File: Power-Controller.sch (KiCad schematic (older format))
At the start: 41 parts, among them P1 USB_B, U1 FT232H, U2 93LC56BT-I/OT, U3 ACPL-247-500E, U4 ACPL-247-500E, Y1 12MHz

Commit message: Change the footprint of 4.7uF capacitors to 1206 to conform to the other circuits (This size of the footprint is used since 2015)
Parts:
- C11, C13, C15, C17: footprint Capacitors_SMD:C_0603 -> SMD_Packages:SMD-1206_Pol
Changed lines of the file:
@@
 F 0 "C17" H 5110 2470 50  0000 L CNN
 F 1 "4.7uF" H 5110 2320 50  0000 L CNN
-F 2 "Capacitors_SMD:C_0603" H 5100 2400 50  0001 C CNN
+F 2 "SMD_Packages:SMD-1206_Pol" H 5100 2400 50  0001 C CNN
 F 3 "" H 5100 2400 50  0000 C CNN
 	1    5100 2400
@@
 F 0 "C11" H 3410 2870 50  0000 L CNN
 F 1 "4.7uF" H 3410 2720 50  0000 L CNN
-F 2 "Capacitors_SMD:C_0603" H 3400 2800 50  0001 C CNN
+F 2 "SMD_Packages:SMD-1206_Pol" H 3400 2800 50  0001 C CNN
 F 3 "" H 3400 2800 50  0000 C CNN
 	1    3400 2800
@@
 F 0 "C15" H 5110 1970 50  0000 L CNN
 F 1 "4.7uF" H 5110 1820 50  0000 L CNN
-F 2 "Capacitors_SMD:C_0603" H 5100 1900 50  0001 C CNN
+F 2 "SMD_Packages:SMD-1206_Pol" H 5100 1900 50  0001 C CNN
 F 3 "" H 5100 1900 50  0000 C CNN
 	1    5100 1900
@@
 F 0 "C13" H 4160 1970 50  0000 L CNN
 F 1 "4.7uF" H 4160 1820 50  0000 L CNN
-F 2 "Capacitors_SMD:C_0603" H 4150 1900 50  0001 C CNN
+F 2 "SMD_Packages:SMD-1206_Pol" H 4150 1900 50  0001 C CNN
 F 3 "" H 4150 1900 50  0000 C CNN
 	1    4150 1900

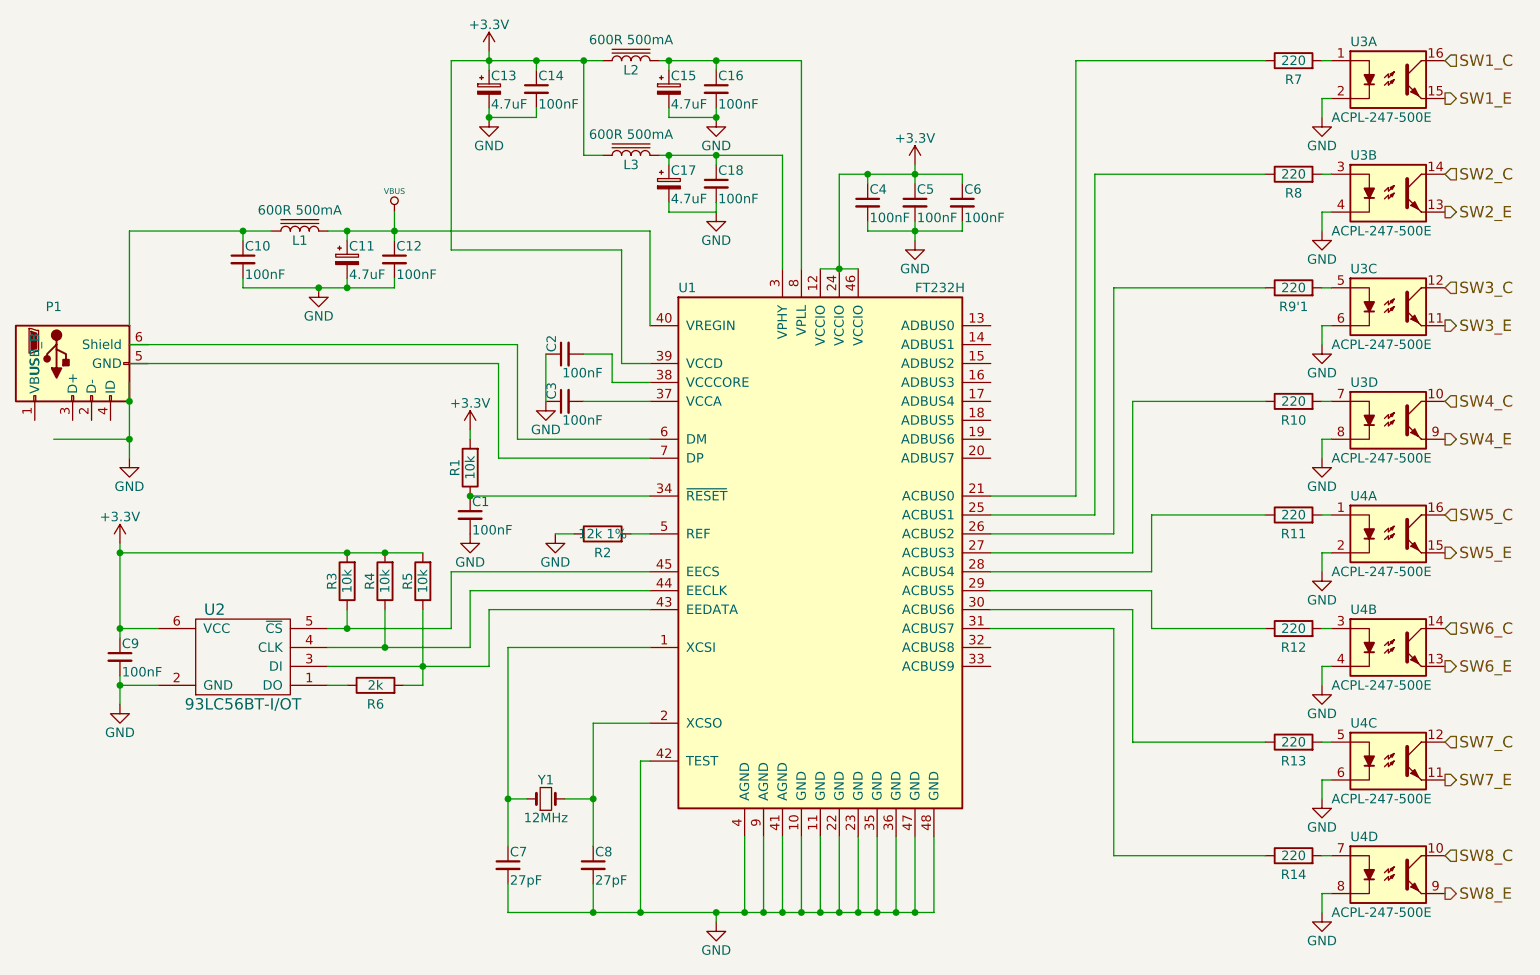
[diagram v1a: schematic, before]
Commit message: Change some R values and C footprints to conform with the Peripheral Bridge module.
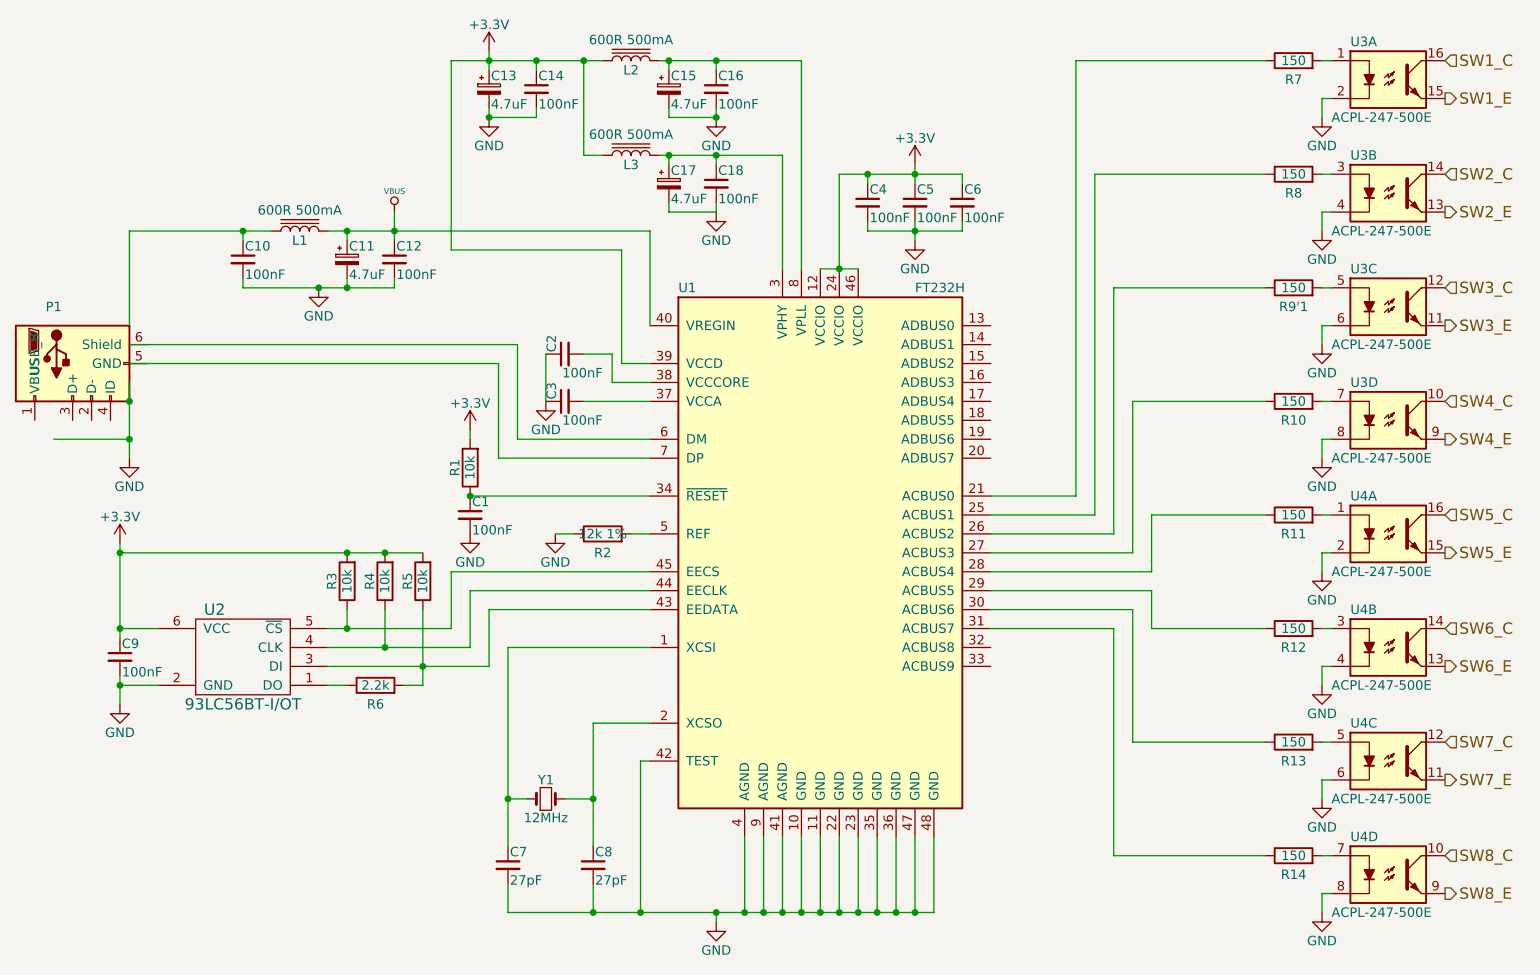
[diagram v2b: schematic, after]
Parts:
- C11: footprint SMD_Packages:SMD-1206_Pol -> MMZ1608S601A-CT
- C13, C15, C17: footprint SMD_Packages:SMD-1206_Pol -> Capacitors_SMD:C_0805
- R10, R11, R12, R13, R14, R7, R8, R9'1: value 220 -> 150
- R6: value 2k -> 2.2k
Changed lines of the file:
@@
 P 3550 5050
 F 0 "R6" V 3450 5050 50  0000 C CNN
-F 1 "2k" V 3550 5050 50  0000 C CNN
+F 1 "2.2k" V 3550 5050 50  0000 C CNN
 F 2 "Resistors_SMD:R_0603" V 3480 5050 30  0001 C CNN
 F 3 "" H 3550 5050 30  0000 C CNN
@@
 F 0 "C17" H 5110 2470 50  0000 L CNN
 F 1 "4.7uF" H 5110 2320 50  0000 L CNN
-F 2 "SMD_Packages:SMD-1206_Pol" H 5100 2400 50  0001 C CNN
+F 2 "Capacitors_SMD:C_0805" H 5100 2400 50  0001 C CNN
 F 3 "" H 5100 2400 50  0000 C CNN
 	1    5100 2400
@@
 F 0 "C11" H 3410 2870 50  0000 L CNN
 F 1 "4.7uF" H 3410 2720 50  0000 L CNN
-F 2 "SMD_Packages:SMD-1206_Pol" H 3400 2800 50  0001 C CNN
+F 2 "MMZ1608S601A-CT" H 3400 2800 50  0001 C CNN
 F 3 "" H 3400 2800 50  0000 C CNN
 	1    3400 2800
@@
 F 0 "C15" H 5110 1970 50  0000 L CNN
 F 1 "4.7uF" H 5110 1820 50  0000 L CNN
-F 2 "SMD_Packages:SMD-1206_Pol" H 5100 1900 50  0001 C CNN
+F 2 "Capacitors_SMD:C_0805" H 5100 1900 50  0001 C CNN
 F 3 "" H 5100 1900 50  0000 C CNN
 	1    5100 1900
@@
 F 0 "C13" H 4160 1970 50  0000 L CNN
 F 1 "4.7uF" H 4160 1820 50  0000 L CNN
-F 2 "SMD_Packages:SMD-1206_Pol" H 4150 1900 50  0001 C CNN
+F 2 "Capacitors_SMD:C_0805" H 4150 1900 50  0001 C CNN
 F 3 "" H 4150 1900 50  0000 C CNN
 	1    4150 1900
@@
 P 8400 4150
 F 0 "R11" V 8300 4150 50  0000 C CNN
-F 1 "220" V 8400 4150 50  0000 C CNN
+F 1 "150" V 8400 4150 50  0000 C CNN
 F 2 "Resistors_SMD:R_0603" V 8330 4150 30  0001 C CNN
 F 3 "" H 8400 4150 30  0000 C CNN
@@
 P 8400 4750
 F 0 "R12" V 8300 4750 50  0000 C CNN
-F 1 "220" V 8400 4750 50  0000 C CNN
+F 1 "150" V 8400 4750 50  0000 C CNN
 F 2 "Resistors_SMD:R_0603" V 8330 4750 30  0001 C CNN
 F 3 "" H 8400 4750 30  0000 C CNN
@@
 P 8400 5350
 F 0 "R13" V 8300 5350 50  0000 C CNN
-F 1 "220" V 8400 5350 50  0000 C CNN
+F 1 "150" V 8400 5350 50  0000 C CNN
 F 2 "Resistors_SMD:R_0603" V 8330 5350 30  0001 C CNN
 F 3 "" H 8400 5350 30  0000 C CNN
@@
 P 8400 5950
 F 0 "R14" V 8300 5950 50  0000 C CNN
-F 1 "220" V 8400 5950 50  0000 C CNN
+F 1 "150" V 8400 5950 50  0000 C CNN
 F 2 "Resistors_SMD:R_0603" V 8330 5950 30  0001 C CNN
 F 3 "" H 8400 5950 30  0000 C CNN
@@
 P 8400 1750
 F 0 "R7" V 8300 1750 50  0000 C CNN
-F 1 "220" V 8400 1750 50  0000 C CNN
+F 1 "150" V 8400 1750 50  0000 C CNN
 F 2 "Resistors_SMD:R_0603" V 8330 1750 30  0001 C CNN
 F 3 "" H 8400 1750 30  0000 C CNN
@@
 P 8400 2350
 F 0 "R8" V 8300 2350 50  0000 C CNN
-F 1 "220" V 8400 2350 50  0000 C CNN
+F 1 "150" V 8400 2350 50  0000 C CNN
 F 2 "Resistors_SMD:R_0603" V 8330 2350 30  0001 C CNN
 F 3 "" H 8400 2350 30  0000 C CNN
@@
 P 8400 2950
 F 0 "R9'1" V 8300 2950 50  0000 C CNN
-F 1 "220" V 8400 2950 50  0000 C CNN
+F 1 "150" V 8400 2950 50  0000 C CNN
 F 2 "Resistors_SMD:R_0603" V 8330 2950 30  0001 C CNN
 F 3 "" H 8400 2950 30  0000 C CNN
@@
 P 8400 3550
 F 0 "R10" V 8300 3550 50  0000 C CNN
-F 1 "220" V 8400 3550 50  0000 C CNN
+F 1 "150" V 8400 3550 50  0000 C CNN
 F 2 "Resistors_SMD:R_0603" V 8330 3550 30  0001 C CNN
 F 3 "" H 8400 3550 30  0000 C CNN
